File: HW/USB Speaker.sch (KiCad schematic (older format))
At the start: 43 parts, among them J1 USB_OTG, J2 TP, J3 TP, Q1 Q_NMOS_DGS, U1 PCM2707C, Y1 12 MHz

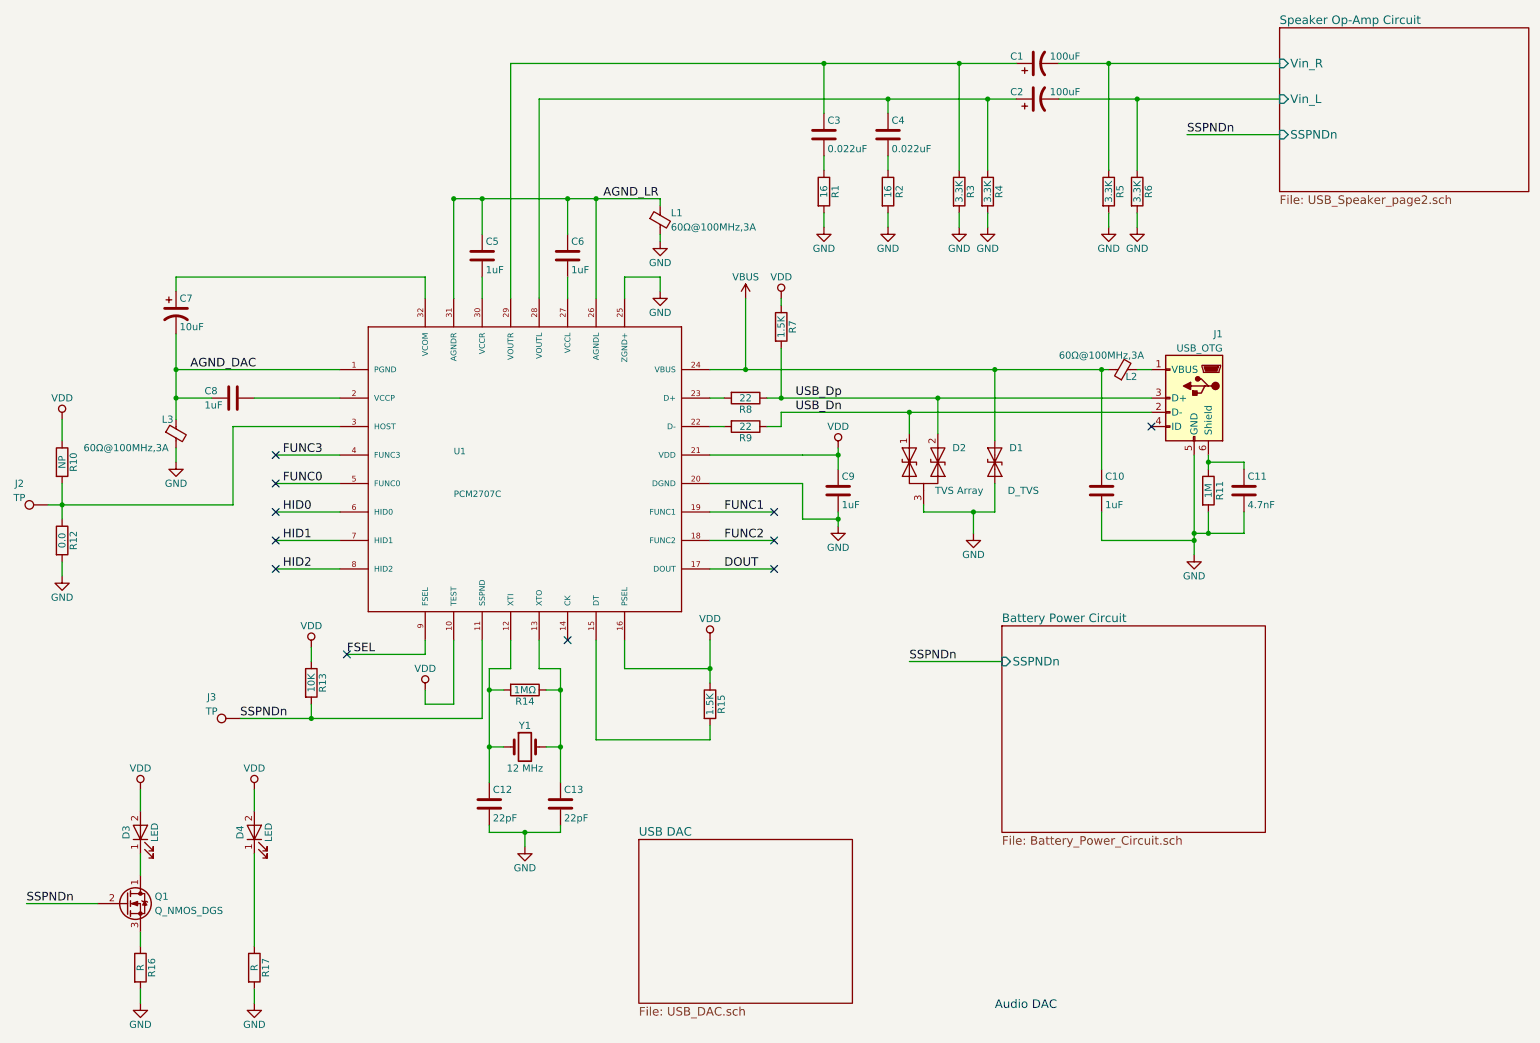
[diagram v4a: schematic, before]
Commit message: Deleted an empty page
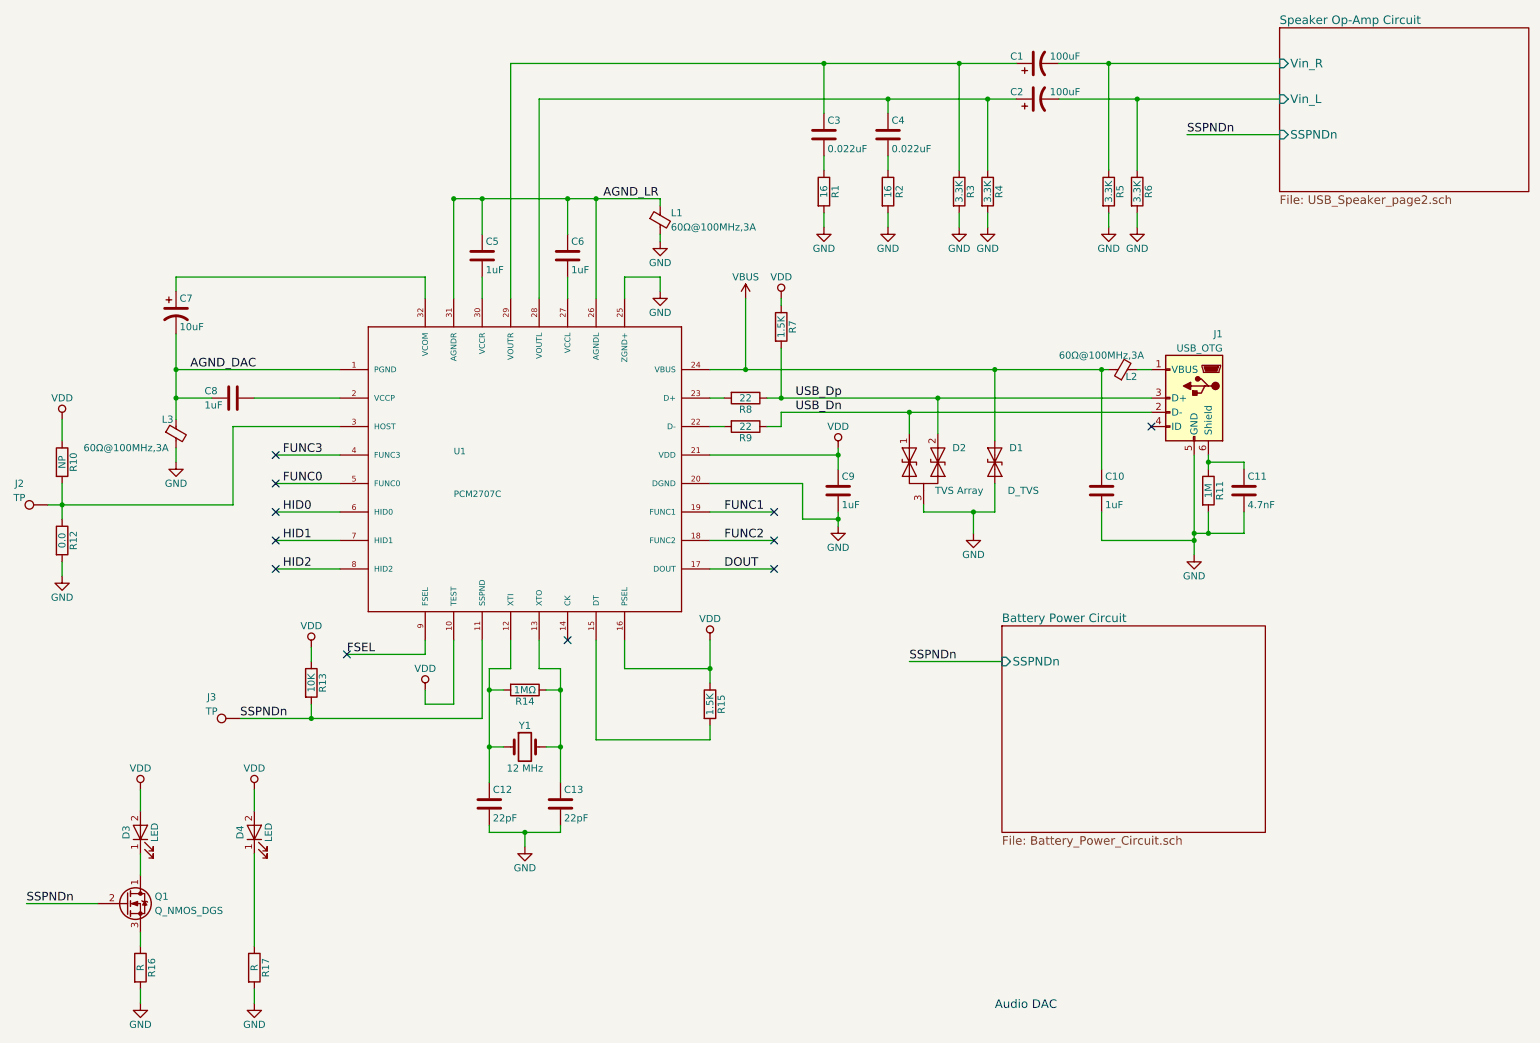
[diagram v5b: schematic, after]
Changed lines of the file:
@@
 	3850 5100 4000 5100
 Wire Wire Line
-	3850 5100 3850 5250
-Wire Wire Line
-	3850 5250 3850 5650
-Wire Wire Line
-	3850 5650 3850 5900
+	3850 5100 3850 5900
 Wire Wire Line
 	4350 5650 4250 5650
@@
 	4100 6350 4100 6250
 Wire Wire Line
-	3850 6250 4100 6250
-Wire Wire Line
-	4100 6250 4350 6250
+	3850 6250 4350 6250
 Wire Wire Line
 	3850 6250 3850 6200
@@
 Connection ~ 4100 6250
 Wire Wire Line
-	4350 5100 4350 5250
-Wire Wire Line
-	4350 5250 4350 5650
-Wire Wire Line
-	4350 5650 4350 5900
-Wire Wire Line
-	8800 3600 8800 4150
-Wire Wire Line
-	8800 4150 8800 4200
-Wire Wire Line
-	8800 4200 8800 4300
-Wire Wire Line
-	8800 4150 8900 4150
-Wire Wire Line
-	8900 4150 9150 4150
-Wire Wire Line
-	8900 3600 8900 3650
-Wire Wire Line
-	8900 3650 8900 3700
+	4350 5100 4350 5900
+Wire Wire Line
+	8800 3600 8800 4300
+Wire Wire Line
+	8800 4150 9150 4150
+Wire Wire Line
+	8900 3600 8900 3700
 Wire Wire Line
 	8900 4150 8900 4000
@@
 	8500 3000 8400 3000
 Wire Wire Line
-	5400 3000 5650 3000
-Wire Wire Line
-	5650 3000 7400 3000
-Wire Wire Line
-	7400 3000 8150 3000
-Wire Wire Line
-	8150 3000 8200 3000
+	5400 3000 8200 3000
 Wire Wire Line
 	8150 3700 8150 3000
@@
 	8150 4200 8800 4200
 Wire Wire Line
-	3600 1800 3800 1800
-Wire Wire Line
-	3800 1800 4400 1800
-Wire Wire Line
-	4400 1800 4600 1800
-Wire Wire Line
-	4600 1800 5050 1800
+	3600 1800 5050 1800
 Wire Wire Line
 	3600 1800 3600 2500
@@
 Connection ~ 3800 1800
 Wire Wire Line
-	1650 2750 1650 3000
-Wire Wire Line
-	1650 3000 1650 3200
-Wire Wire Line
-	1650 3200 1650 3350
+	1650 2750 1650 3350
 Wire Wire Line
 	1900 3200 1650 3200
@@
 	4800 5100 5400 5100
 Wire Wire Line
-	5400 4900 5400 5100
-Wire Wire Line
-	5400 5100 5400 5200
+	5400 4900 5400 5200
 Wire Wire Line
 	2200 3200 2800 3200
@@
 	5400 5600 5400 5500
 Wire Wire Line
-	6300 3550 6300 3600
-Wire Wire Line
-	6300 3600 6300 3700
-Wire Wire Line
-	6300 3600 6050 3600
-Wire Wire Line
-	6050 3600 6050 3600
-Wire Wire Line
-	6050 3600 5400 3600
+	6300 3550 6300 3700
+Wire Wire Line
+	5400 3600 6300 3600
 Connection ~ 6300 3600
 Wire Wire Line
 	6050 3800 6050 4050
 Wire Wire Line
-	6300 4000 6300 4050
-Wire Wire Line
-	6300 4050 6300 4100
+	6300 4000 6300 4100
 Wire Wire Line
 	6050 4050 6300 4050
@@
 	5400 3400 5500 3400
 Wire Wire Line
-	5800 3200 5900 3200
-Wire Wire Line
-	5900 3200 7000 3200
-Wire Wire Line
-	7000 3200 8500 3200
+	5800 3200 8500 3200
 Wire Wire Line
 	5800 3400 5900 3400
@@
 	5900 3400 5900 3300
 Wire Wire Line
-	5900 3300 6800 3300
-Wire Wire Line
-	6800 3300 8500 3300
+	5900 3300 8500 3300
 Wire Wire Line
 	3600 4900 3600 5350
@@
 	4000 850  4000 2500
 Wire Wire Line
-	4000 850  6200 850
-Wire Wire Line
-	6200 850  7150 850
-Wire Wire Line
-	7150 850  7550 850
+	4000 850  7550 850
 Wire Wire Line
 	4200 1100 4200 2500
 Wire Wire Line
-	4200 1100 6650 1100
-Wire Wire Line
-	6650 1100 7350 1100
-Wire Wire Line
-	7350 1100 7550 1100
-Wire Wire Line
-	7850 850  8200 850
-Wire Wire Line
-	8200 850  9400 850
-Wire Wire Line
-	7850 1100 8400 1100
-Wire Wire Line
-	8400 1100 9400 1100
+	4200 1100 7550 1100
+Wire Wire Line
+	7850 850  9400 850
+Wire Wire Line
+	7850 1100 9400 1100
 Wire Wire Line
 	6200 1200 6200 850
@@
 	3800 5450 3800 4900
 Wire Wire Line
-	2100 5450 2600 5450
-Wire Wire Line
-	2600 5450 3800 5450
+	2100 5450 3800 5450
 Wire Wire Line
 	2800 3400 2050 3400
 Wire Wire Line
-	2050 3400 2050 3950
-Wire Wire Line
-	850  3800 850  3950
-Wire Wire Line
-	850  3950 850  4050
+	2050 3950 2050 3400
+Wire Wire Line
+	850  3800 850  4050
 $Comp
 L R R10
@@
 $EndComp
 Wire Wire Line
-	2050 3950 850  3950
-Wire Wire Line
-	850  3950 750  3950
+	750  3950 2050 3950
 $Comp
 L TEST_1P J3
@@
 	7400 4000 7400 3800
 Wire Wire Line
-	6900 4000 7250 4000
-Wire Wire Line
-	7250 4000 7400 4000
+	6900 4000 7400 4000
 Wire Wire Line
 	7250 4000 7250 4150
@@
 	6800 3450 6800 3300
 Connection ~ 6800 3300
-$Sheet
-S 4900 6300 1500 1150
-U 5B429541
-F0 "USB DAC" 60
-F1 "USB_DAC.sch" 60
-$EndSheet
 $EndSCHEMATC

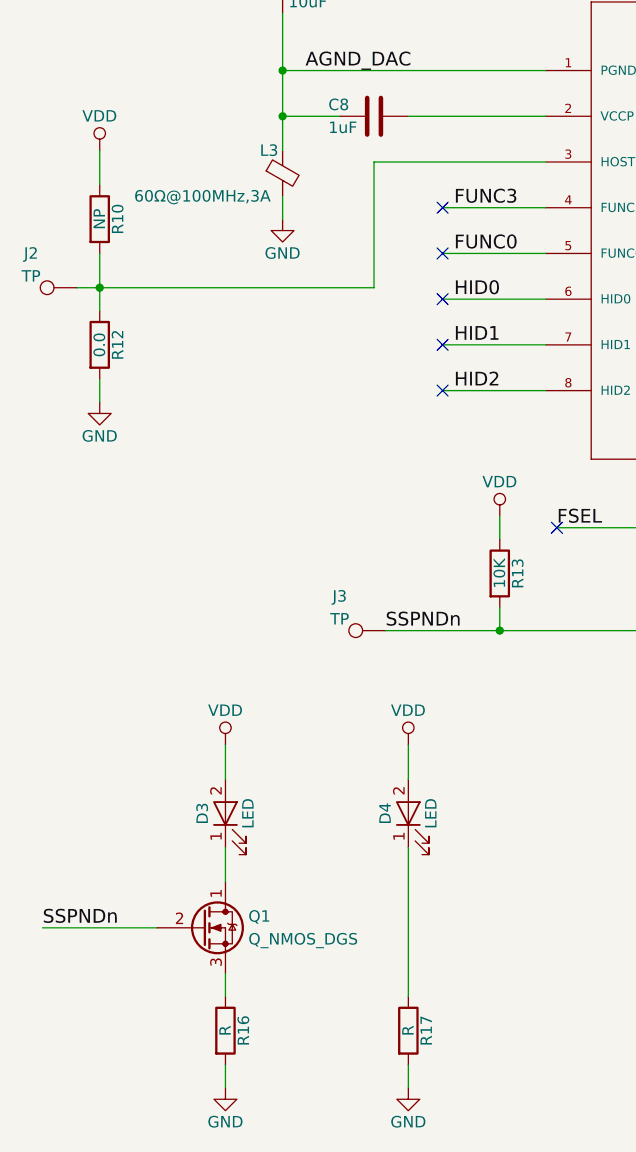
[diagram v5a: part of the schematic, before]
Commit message: 7V Regulator now a 5V buck converter
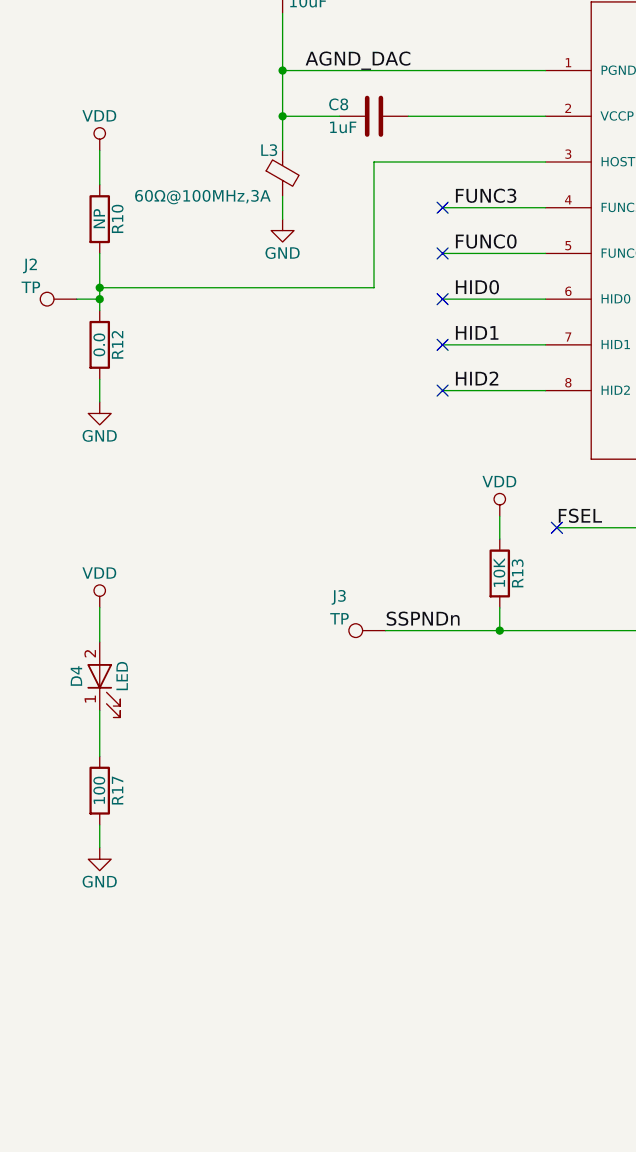
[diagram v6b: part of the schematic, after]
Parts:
- removed D3: LED, symbol LED
- removed Q1: Q_NMOS_DGS, symbol Q_NMOS_DGS
- removed R16: R, symbol R
- R17: value R -> 100
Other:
- moved on the sheet: D4, J2, R17
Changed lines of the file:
@@
 $Descr A4 11693 8268
 encoding utf-8
-Sheet 1 6
+Sheet 1 3
 Title ""
 Date ""
@@
 	2800 3400 2050 3400
 Wire Wire Line
-	2050 3950 2050 3400
+	2050 3400 2050 3950
 Wire Wire Line
 	850  3800 850  4050
@@
 SSPNDn
 $Comp
-L Q_NMOS_DGS Q1
-U 1 1 5B42C852
-P 1300 6750
-F 0 "Q1" H 1500 6800 50  0000 L CNN
-F 1 "Q_NMOS_DGS" H 1500 6700 50  0000 L CNN
-F 2 "" H 1500 6850 50  0001 C CNN
-F 3 "" H 1300 6750 50  0001 C CNN
-	1    1300 6750
-	1    0    0    -1
-$EndComp
-$Comp
-L LED D3
-U 1 1 5B3CEC2F
-P 1400 6250
-F 0 "D3" H 1400 6350 50  0000 C CNN
-F 1 "LED" H 1400 6150 50  0000 C CNN
-F 2 "" H 1400 6250 50  0001 C CNN
-F 3 "" H 1400 6250 50  0001 C CNN
-	1    1400 6250
-	0    -1   -1   0
-$EndComp
-$Comp
-L R R16
-U 1 1 5B3CED96
-P 1400 7200
-F 0 "R16" V 1480 7200 50  0000 C CNN
-F 1 "R" V 1400 7200 50  0000 C CNN
-F 2 "" V 1330 7200 50  0001 C CNN
-F 3 "" H 1400 7200 50  0001 C CNN
-	1    1400 7200
-	1    0    0    -1
-$EndComp
-$Comp
-L GND #PWR24
-U 1 1 5B42C855
-P 1400 7450
-F 0 "#PWR24" H 1400 7200 50  0001 C CNN
-F 1 "GND" H 1400 7300 50  0000 C CNN
-F 2 "" H 1400 7450 50  0001 C CNN
-F 3 "" H 1400 7450 50  0001 C CNN
-	1    1400 7450
-	1    0    0    -1
-$EndComp
-Wire Wire Line
-	1400 6400 1400 6550
-Wire Wire Line
-	1400 6950 1400 7050
-Wire Wire Line
-	1400 7450 1400 7350
-$Comp
-L VDD #PWR21
-U 1 1 5B42C856
-P 1400 5950
-F 0 "#PWR21" H 1400 5800 50  0001 C CNN
-F 1 "VDD" H 1400 6100 50  0000 C CNN
-F 2 "" H 1400 5950 50  0001 C CNN
-F 3 "" H 1400 5950 50  0001 C CNN
-	1    1400 5950
-	1    0    0    -1
-$EndComp
-Wire Wire Line
-	1400 6100 1400 5950
-Wire Wire Line
-	1100 6750 600  6750
-Text Label 600  6750 0    60   ~ 0
-SSPNDn
-$Comp
 L LED D4
 U 1 1 5B3D0088
-P 2200 6250
-F 0 "D4" H 2200 6350 50  0000 C CNN
-F 1 "LED" H 2200 6150 50  0000 C CNN
-F 2 "" H 2200 6250 50  0001 C CNN
-F 3 "" H 2200 6250 50  0001 C CNN
-	1    2200 6250
+P 850 5650
+F 0 "D4" H 850 5750 50  0000 C CNN
+F 1 "LED" H 850 5550 50  0000 C CNN
+F 2 "" H 850 5650 50  0001 C CNN
+F 3 "" H 850 5650 50  0001 C CNN
+	1    850  5650
 	0    -1   -1   0
 $EndComp
-Wire Wire Line
-	2200 6400 2200 7050
 $Comp
 L VDD #PWR22
 U 1 1 5B42C858
-P 2200 5950
-F 0 "#PWR22" H 2200 5800 50  0001 C CNN
-F 1 "VDD" H 2200 6100 50  0000 C CNN
-F 2 "" H 2200 5950 50  0001 C CNN
-F 3 "" H 2200 5950 50  0001 C CNN
-	1    2200 5950
-	1    0    0    -1
-$EndComp
-Wire Wire Line
-	2200 6100 2200 5950
+P 850 5350
+F 0 "#PWR22" H 850 5200 50  0001 C CNN
+F 1 "VDD" H 850 5500 50  0000 C CNN
+F 2 "" H 850 5350 50  0001 C CNN
+F 3 "" H 850 5350 50  0001 C CNN
+	1    850  5350
+	1    0    0    -1
+$EndComp
+Wire Wire Line
+	850  5500 850  5350
 $Comp
 L R R17
 U 1 1 5B42C859
-P 2200 7200
-F 0 "R17" V 2280 7200 50  0000 C CNN
-F 1 "R" V 2200 7200 50  0000 C CNN
-F 2 "" V 2130 7200 50  0001 C CNN
-F 3 "" H 2200 7200 50  0001 C CNN
-	1    2200 7200
+P 850 6150
+F 0 "R17" V 930 6150 50  0000 C CNN
+F 1 "100" V 850 6150 50  0000 C CNN
+F 2 "" V 780 6150 50  0001 C CNN
+F 3 "" H 850 6150 50  0001 C CNN
+	1    850  6150
 	1    0    0    -1
 $EndComp
@@
 L GND #PWR25
 U 1 1 5B42C85A
-P 2200 7450
-F 0 "#PWR25" H 2200 7200 50  0001 C CNN
-F 1 "GND" H 2200 7300 50  0000 C CNN
-F 2 "" H 2200 7450 50  0001 C CNN
-F 3 "" H 2200 7450 50  0001 C CNN
-	1    2200 7450
-	1    0    0    -1
-$EndComp
-Wire Wire Line
-	2200 7450 2200 7350
+P 850 6400
+F 0 "#PWR25" H 850 6150 50  0001 C CNN
+F 1 "GND" H 850 6250 50  0000 C CNN
+F 2 "" H 850 6400 50  0001 C CNN
+F 3 "" H 850 6400 50  0001 C CNN
+	1    850  6400
+	1    0    0    -1
+$EndComp
+Wire Wire Line
+	850  6400 850  6300
 $Comp
 L TEST_1P J2
 U 1 1 5B3D30CC
-P 750 3950
-F 0 "J2" V 900 4150 50  0000 C CNN
-F 1 "TP" V 800 4150 50  0000 C CNN
-F 2 "" H 950 3950 50  0001 C CNN
-F 3 "" H 950 3950 50  0001 C CNN
-	1    750  3950
+P 750 4000
+F 0 "J2" V 900 4200 50  0000 C CNN
+F 1 "TP" V 800 4200 50  0000 C CNN
+F 2 "" H 950 4000 50  0001 C CNN
+F 3 "" H 950 4000 50  0001 C CNN
+	1    750  4000
 	0    -1   -1   0
 $EndComp
 Wire Wire Line
-	750  3950 2050 3950
+	2050 3950 850  3950
 $Comp
 L TEST_1P J3
@@
 	6800 3450 6800 3300
 Connection ~ 6800 3300
+Wire Wire Line
+	750  4000 850  4000
+Connection ~ 850  4000
+Wire Wire Line
+	850  6000 850  5800
 $EndSCHEMATC

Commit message: Buck and fp
Changed buck to one with 3A output. Started fp association
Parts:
- J2, J3: footprint (none) -> Measurement_Points:Measurement_Point_Round-TH_Big
- L1, L2, L3: footprint (none) -> Inductors_SMD:L_0805_HandSoldering
- R1, R10, R11, R12, R13, R14, R15, R17, R2, R3, R4, R5, R6, R7, R8, R9: footprint (none) -> Resistors_SMD:R_0805_HandSoldering
- U1: footprint PCM2707C -> Housings_QFP:TQFP-32_7x7mm_Pitch0.8mm
